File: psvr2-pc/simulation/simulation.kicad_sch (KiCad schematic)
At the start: 31 parts, among them Q1 PMOS, Q2 PMOS, Q3 NPN, Q4 PMOS, Q5 PMOS, Q6 NPN, Q8 PMOS

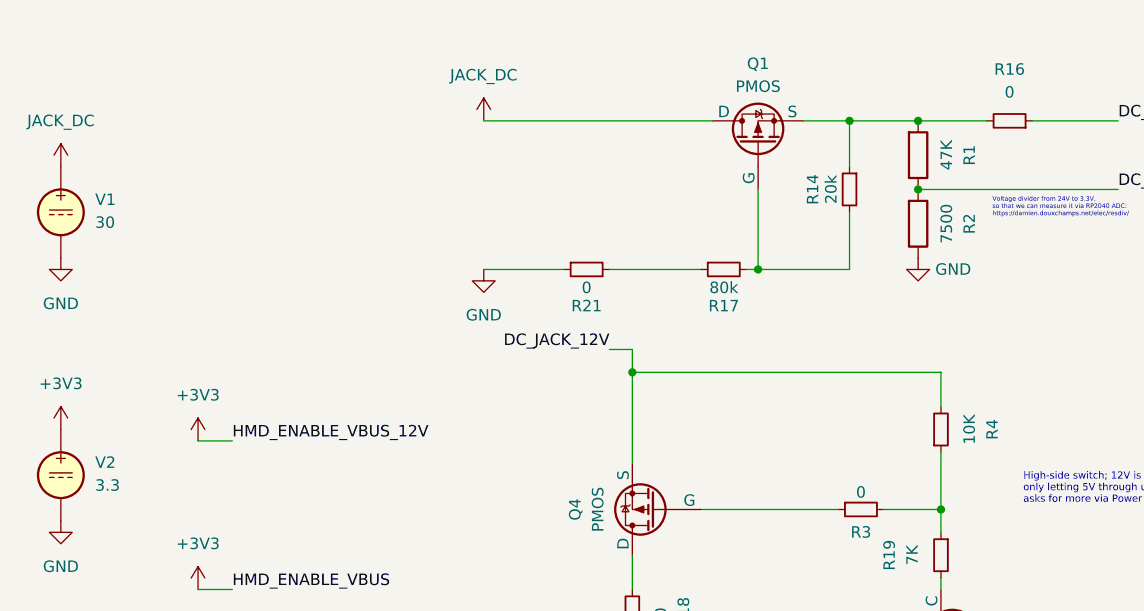
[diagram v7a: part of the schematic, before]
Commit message: Add a bunch of to-do notes in the schematic. Mess with trying to simulate a TVS diode.
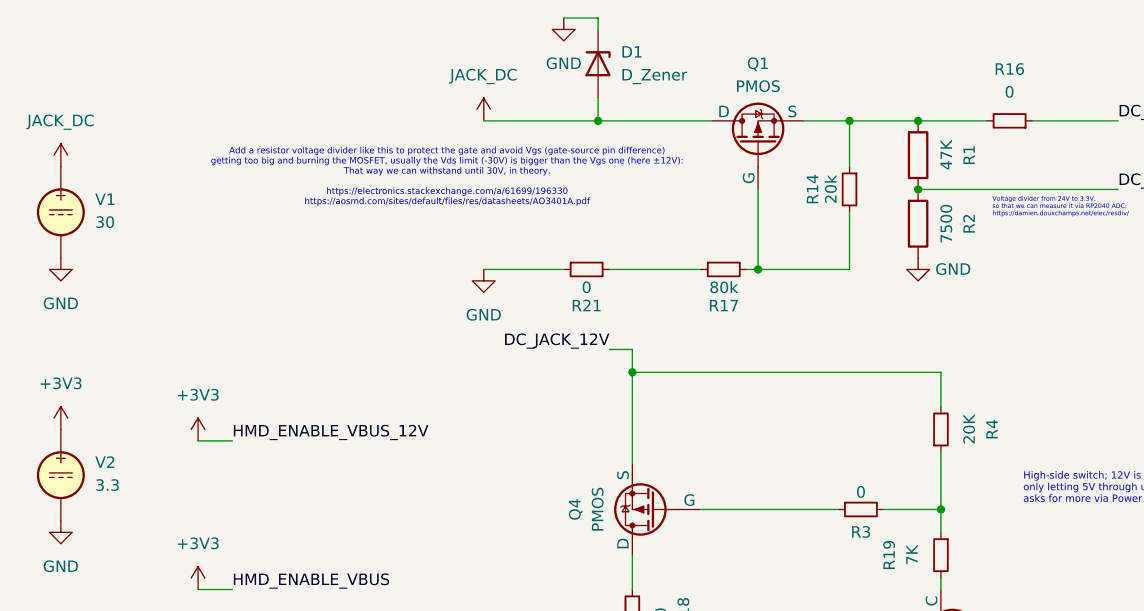
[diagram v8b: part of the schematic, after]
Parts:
- added D1: D_Zener, symbol Device:D_Zener
- R4: value 10K -> 20K
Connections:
- net GND: now also D1.1 (K)
- net JACK_DC: now also D1.2 (A)
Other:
- note added: "Add a resistor voltage divider like this to protect the gate and avoid Vgs (gate-source pin difference) getting too big and burning the MOSFET, usually the Vds limit (-30V) is bigger than the Vgs one (here ±12V): That way we can withstand until 30V, in theory. https://electronics.stackexchange.com/a/61699/196330 https://aosmd.com/sites/default/files/res/datasheets/AO3401A.pdf"
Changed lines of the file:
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@@
+	)
+	(junction
+		(at 81.28 21.59)
+		(diameter 0)
+		(color 0 0 0 0)
 	)
 	(junction
@@
 	(wire
 		(pts
-			(xy 68.58 21.59) (xy 93.98 21.59)
+			(xy 68.58 21.59) (xy 81.28 21.59)
 		)
 		(stroke
@@
 	(wire
 		(pts
+			(xy 77.47 10.16) (xy 81.28 10.16)
+		)
+		(stroke
+			(width 0)
+			(type default)
+		)
+	)
+	(wire
+		(pts
 			(xy 165.1 146.05) (xy 168.91 146.05)
 		)
@@
 	(wire
 		(pts
+			(xy 81.28 19.05) (xy 81.28 21.59)
+		)
+		(stroke
+			(width 0)
+			(type default)
+		)
+	)
+	(wire
+		(pts
 			(xy 85.09 78.74) (xy 85.09 83.82)
 		)
@@
 		(pts
 			(xy 146.05 78.74) (xy 149.86 78.74)
+		)
+		(stroke
+			(width 0)
+			(type default)
+		)
+	)
+	(wire
+		(pts
+			(xy 81.28 10.16) (xy 81.28 11.43)
+		)
+		(stroke
+			(width 0)
+			(type default)
+		)
+	)
+	(wire
+		(pts
+			(xy 81.28 21.59) (xy 93.98 21.59)
 		)
 		(stroke
@@
 			)
 			(justify left bottom)
+		)
+	)
+	(text "Add a resistor voltage divider like this to protect the gate and avoid Vgs (gate-source pin difference)\ngetting too big and burning the MOSFET, usually the Vds limit (-30V) is bigger than the Vgs one (here ±12V):\nThat way we can withstand until 30V, in theory.\n\nhttps://electronics.stackexchange.com/a/61699/196330\nhttps://aosmd.com/sites/default/files/res/datasheets/AO3401A.pdf"
+		(exclude_from_sim no)
+		(at 64.516 27.94 0)
+		(effects
+			(font
+				(size 0.7 0.7)
+			)
 		)
 	)
@@
 	)
 	(symbol
+		(lib_id "power:GND")
+		(at 77.47 10.16 0)
+		(unit 1)
+		(exclude_from_sim no)
+		(in_bom yes)
+		(on_board yes)
+		(dnp no)
+		(fields_autoplaced yes)
+		(property "Reference" "#PWR018"
+			(at 77.47 16.51 0)
+			(effects
+				(font
+					(size 1.27 1.27)
+				)
+				(hide yes)
+			)
+		)
+		(property "Value" "GND"
+			(at 77.47 15.24 0)
+			(effects
+				(font
+					(size 1.27 1.27)
+				)
+			)
+		)
+		(property "Footprint" ""
+			(at 77.47 10.16 0)
+			(effects
+				(font
+					(size 1.27 1.27)
+				)
+				(hide yes)
+			)
+		)
+		(property "Datasheet" ""
+			(at 77.47 10.16 0)
+			(effects
+				(font
+					(size 1.27 1.27)
+				)
+				(hide yes)
+			)
+		)
+		(property "Description" "Power symbol creates a global label with name \"GND\" , ground"
+			(at 77.47 10.16 0)
+			(effects
+				(font
+					(size 1.27 1.27)
+				)
+				(hide yes)
+			)
+		)
+		(pin "1"
+		)
+		(instances
+			(project "simulation"
+				(path "/f11bb3d3-5794-4a95-b9a9-d0bd9f1c0d65"
+					(reference "#PWR018")
+					(unit 1)
+				)
+			)
+		)
+	)
+	(symbol
 		(lib_id "Simulation_SPICE:VDC")
 		(at 21.59 60.96 0)
@@
 	)
 	(symbol
+		(lib_id "Device:D_Zener")
+		(at 81.28 15.24 270)
+		(unit 1)
+		(exclude_from_sim no)
+		(in_bom yes)
+		(on_board yes)
+		(dnp no)
+		(fields_autoplaced yes)
+		(property "Reference" "D1"
+			(at 83.82 13.9699 90)
+			(effects
+				(font
+					(size 1.27 1.27)
+				)
+				(justify left)
+			)
+		)
+		(property "Value" "D_Zener"
+			(at 83.82 16.5099 90)
+			(effects
+				(font
+					(size 1.27 1.27)
+				)
+				(justify left)
+			)
+		)
+		(property "Footprint" ""
+			(at 81.28 15.24 0)
+			(effects
+				(font
+					(size 1.27 1.27)
+				)
+				(hide yes)
+			)
+		)
+		(property "Datasheet" "~"
+			(at 81.28 15.24 0)
+			(effects
+				(font
+					(size 1.27 1.27)
+				)
+				(hide yes)
+			)
+		)
+		(property "Description" "Zener diode"
+			(at 81.28 15.24 0)
+			(effects
+				(font
+					(size 1.27 1.27)
+				)
+				(hide yes)
+			)
+		)
+		(property "Sim.Device" "D"
+			(at 81.28 15.24 0)
+			(effects
+				(font
+					(size 1.27 1.27)
+				)
+				(hide yes)
+			)
+		)
+		(property "Sim.Pins" "1=K, 2=A"
+			(at 81.28 15.24 0)
+			(effects
+				(font
+					(size 1.27 1.27)
+				)
+				(hide yes)
+			)
+		)
+		(pin "2"
+		)
+		(pin "1"
+		)
+		(instances
+			(project "simulation"
+				(path "/f11bb3d3-5794-4a95-b9a9-d0bd9f1c0d65"
+					(reference "D1")
+					(unit 1)
+				)
+			)
+		)
+	)
+	(symbol
 		(lib_id "Device:R_Small")
 		(at 119.38 55.88 0)
@@
 			)
 		)
-		(property "Value" "10K"
+		(property "Value" "20K"
 			(at 122.555 55.88 90)
 			(effects
